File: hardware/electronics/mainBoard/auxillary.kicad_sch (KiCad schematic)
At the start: 44 parts, among them J10 Bus_M.2_Socket_E, J11 M.2 Standoff, J12 M.2 Standoff, SW7 JS102011JCQN, SW8 JS102011JCQN, U14 TPS22996H-Q1, U15 TXS0108EQWRKSRQ1, U16 TXS0104VxRUTR

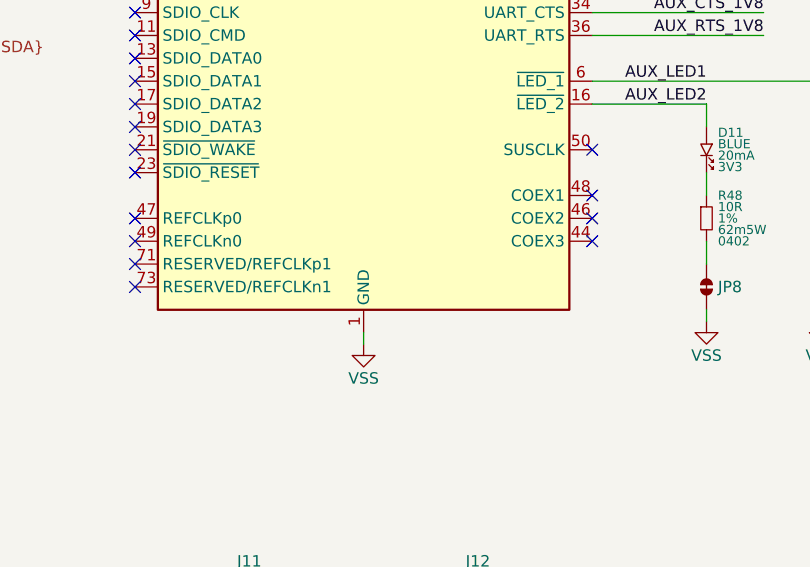
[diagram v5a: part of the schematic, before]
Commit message: added footprints to symbols
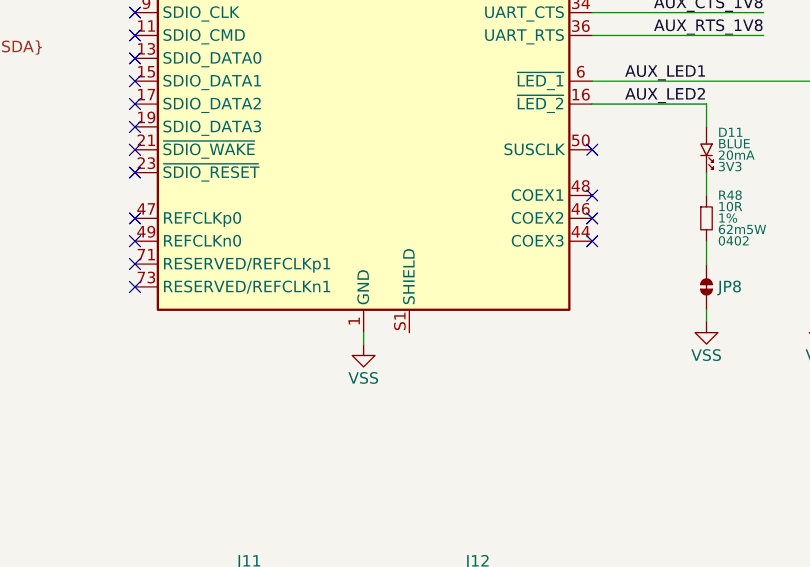
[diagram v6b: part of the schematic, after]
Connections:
- new net: J10.S1 (SHIELD), J10.S2 (SHIELD)
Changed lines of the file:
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@@
 		(pin "53"
+		)
+		(pin "S1"
+		)
+		(pin "S2"
 		)
 		(instances

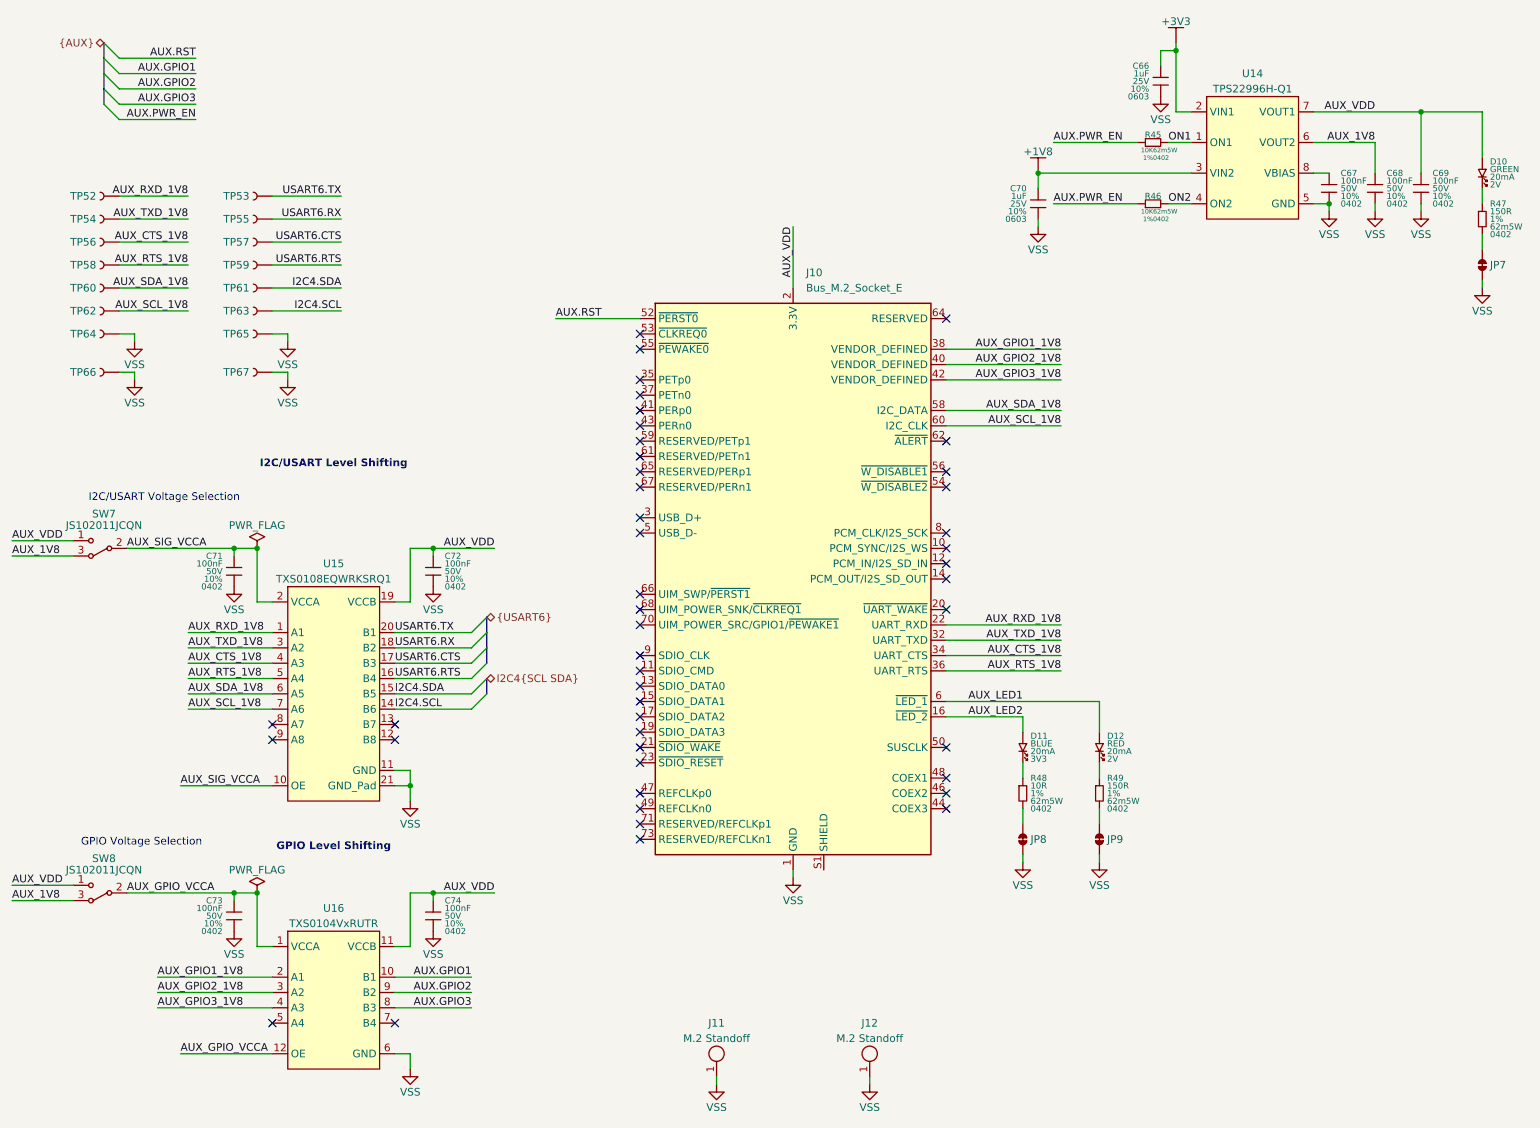
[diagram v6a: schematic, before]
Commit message: assigned footprints
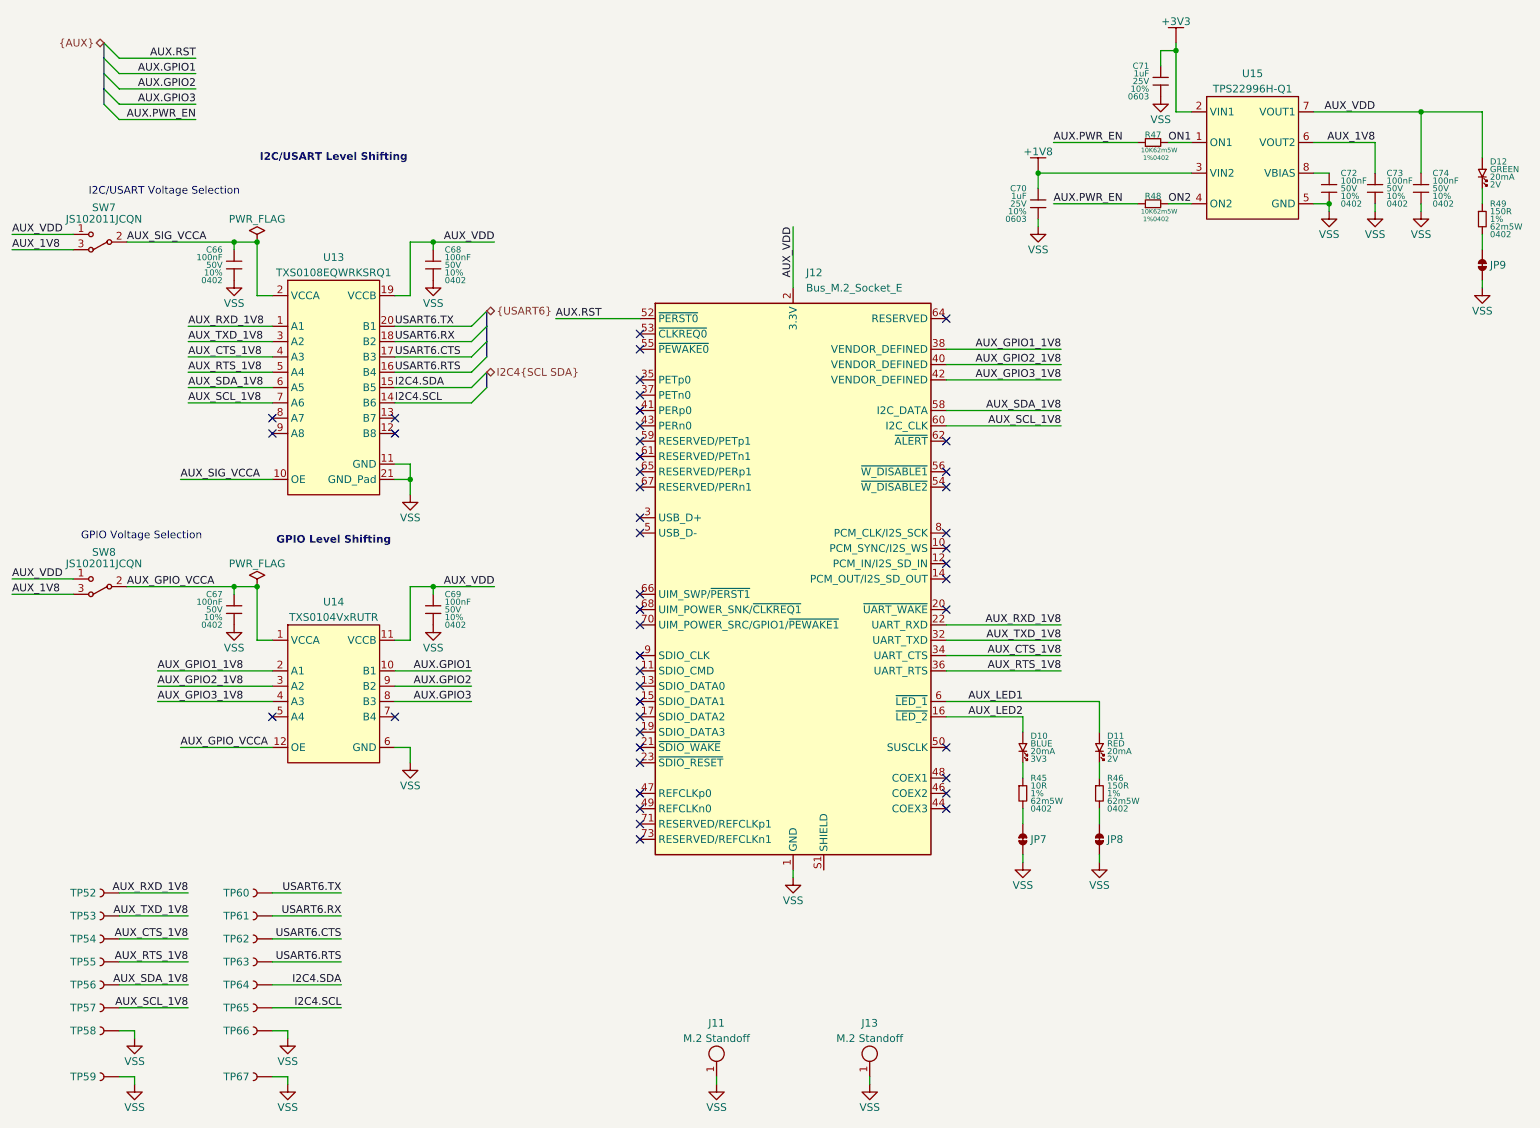
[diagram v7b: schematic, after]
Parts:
- C66: renamed from C71; footprint (none) -> lib_passives:GCM0402
- C67: renamed from C73; footprint (none) -> lib_passives:GCM0402
- C68: renamed from C72; footprint (none) -> lib_passives:GCM0402
- C69: renamed from C74; footprint (none) -> lib_passives:GCM0402
- C70: footprint (none) -> lib_passives:GRT0603
- C71: renamed from C66; footprint (none) -> lib_passives:GRT0603
- C72: renamed from C67; footprint (none) -> lib_passives:GCM0402
- C73: renamed from C68; footprint (none) -> lib_passives:GCM0402
- C74: renamed from C69; footprint (none) -> lib_passives:GCM0402
- D10: renamed from D11; footprint (none) -> lib_diodes:LTST-0603
- D11: renamed from D12; footprint (none) -> lib_diodes:LTST-0603
- D12: renamed from D10; footprint (none) -> lib_diodes:LTST-0603
- J11: footprint (none) -> lib_misc:MountingHole_3.5mm_Pad_Via
- J13: renamed from J12; footprint (none) -> lib_misc:MountingHole_3.5mm_Pad_Via
- JP7: renamed from JP8; footprint (none) -> lib_misc:SolderJumper-2_P1.3mm_Bridged_RoundedPad1.0x1.5mm
- JP8: renamed from JP9; footprint (none) -> lib_misc:SolderJumper-2_P1.3mm_Bridged_RoundedPad1.0x1.5mm
- JP9: renamed from JP7; footprint (none) -> lib_misc:SolderJumper-2_P1.3mm_Bridged_RoundedPad1.0x1.5mm
- R45: renamed from R48; footprint (none) -> lib_passives:CRCW0402
- R46: renamed from R49; footprint (none) -> lib_passives:CRCW0402
- R47: renamed from R45; footprint (none) -> lib_passives:CRCW0402
- R48: renamed from R46; footprint (none) -> lib_passives:CRCW0402
- R49: renamed from R47; footprint (none) -> lib_passives:CRCW0402
- TP52: footprint (none) -> lib_misc:TP_2mm
- TP53: renamed from TP54; footprint (none) -> lib_misc:TP_2mm
- TP54: renamed from TP56; footprint (none) -> lib_misc:TP_2mm
- TP55: renamed from TP58; footprint (none) -> lib_misc:TP_2mm
- TP56: renamed from TP60; footprint (none) -> lib_misc:TP_2mm
- TP57: renamed from TP62; footprint (none) -> lib_misc:TP_2mm
- TP58: renamed from TP64; footprint (none) -> lib_misc:TP_RCW
- TP59: renamed from TP66; footprint (none) -> lib_misc:TP_RCW
- TP60: renamed from TP53; footprint (none) -> lib_misc:TP_2mm
- TP61: renamed from TP55; footprint (none) -> lib_misc:TP_2mm
- TP62: renamed from TP57; footprint (none) -> lib_misc:TP_2mm
- TP63: renamed from TP59; footprint (none) -> lib_misc:TP_2mm
- TP64: renamed from TP61; footprint (none) -> lib_misc:TP_2mm
- TP65: renamed from TP63; footprint (none) -> lib_misc:TP_2mm
- TP66: renamed from TP65; footprint (none) -> lib_misc:TP_RCW
- TP67: footprint (none) -> lib_misc:TP_RCW
- U13: renamed from U15; footprint (none) -> lib_ICs:QFN50P450X250X100-20
- renumbered J10 to J12, U16 to U14, U14 to U15
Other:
- moved on the sheet: C66, C67, C68, C69, SW7, SW8, TP52, TP53, TP54, TP55, TP56, TP57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

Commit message: added UART RX/TX fixer pads for 0R resistors
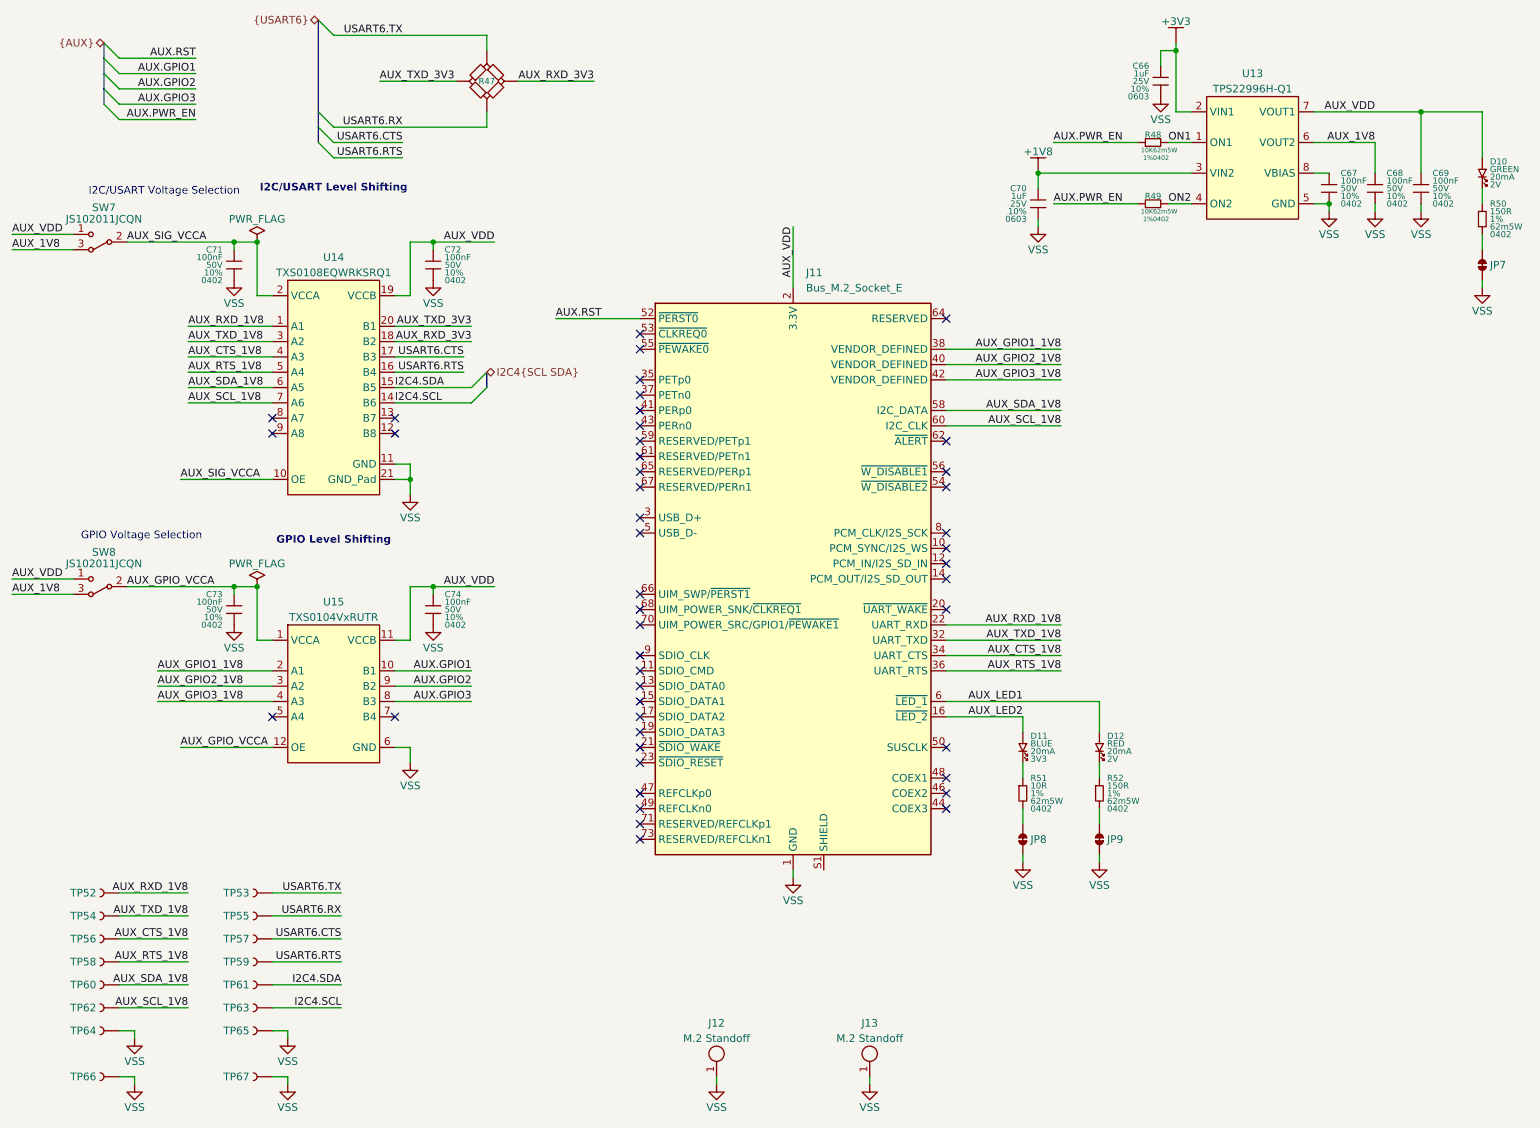
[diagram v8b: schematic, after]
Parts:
- added R47: ~, lib_passives:CRCW0402_QUAD_UART, symbol lib_sch:R_double
- renumbered C71 to C66, C72 to C67, C73 to C68, C74 to C69, C66 to C71, C68 to C72, C67 to C73, C69 to C74, D12 to D10, D10 to D11, D11 to D12, J12 to J11, J11 to J12, JP9 to JP7, JP7 to JP8, JP8 to JP9, R47 to R48, R48 to R49, R49 to R50, R45 to R51, R46 to R52, TP60 to TP53, TP53 to TP54, TP61 to TP55, TP54 to TP56, TP62 to TP57, TP55 to TP58, TP63 to TP59, TP56 to TP60, TP64 to TP61, TP57 to TP62, TP65 to TP63, TP58 to TP64, TP66 to TP65, TP59 to TP66, U15 to U13, U13 to U14, U14 to U15
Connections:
- net USART6.RX: now also R47.3; no longer U14.18 (B2)
- net USART6.TX: now also R47.1; no longer U14.20 (B1)
- new net AUX_RXD_3V3: R47.2, U14.18 (B2)
- new net AUX_TXD_3V3: R47.4, U14.20 (B1)
